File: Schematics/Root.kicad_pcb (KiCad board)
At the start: 2 copper layers, 100 x 100 mm, 132 parts, among them CON1 USB-MICRO-B, IC1 ATXMEGA256A3BU-A, J1 AVR_JTAG_Header, P1 CONN_02X08, U1 PCA9685, U10 PCA9685, U11 PCA9685, U12 PCA9685, U13 LT8612, U2 PCA9685, U3 PCA9685, U4 PCA9685, U5 PCA9685, U6 PCA9685, U7 PCA9685, U8 PCA9685, U9 PCA9685, X1 12MHz, X2 32.768KhZ

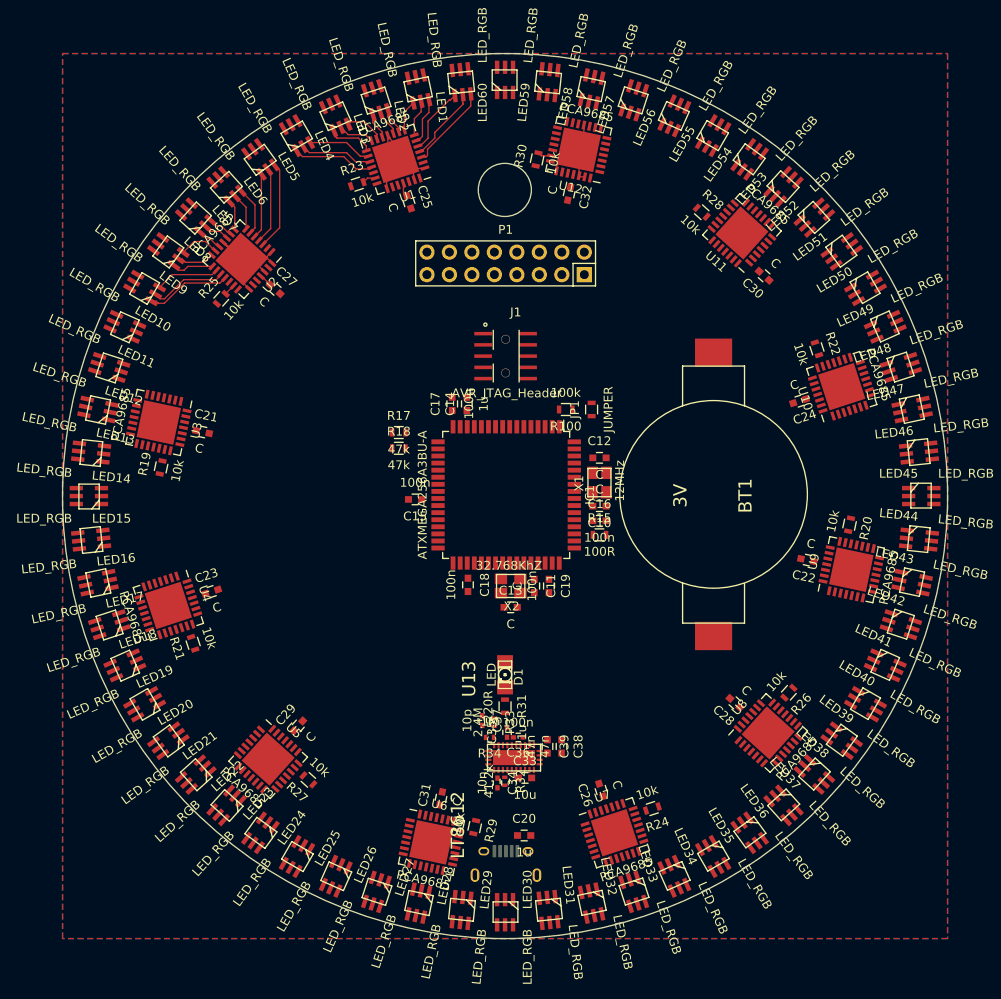
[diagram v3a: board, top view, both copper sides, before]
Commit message: Changed lots
Finalised the Inductor. Closes #5
Changed USB Connector. Closes #4
Added four switches for a simple interface. Closes #7
Added a power jack. Closes #3
Found RTC Oscillator. Closes #1.
Added part numbers to all major components. Closes #2
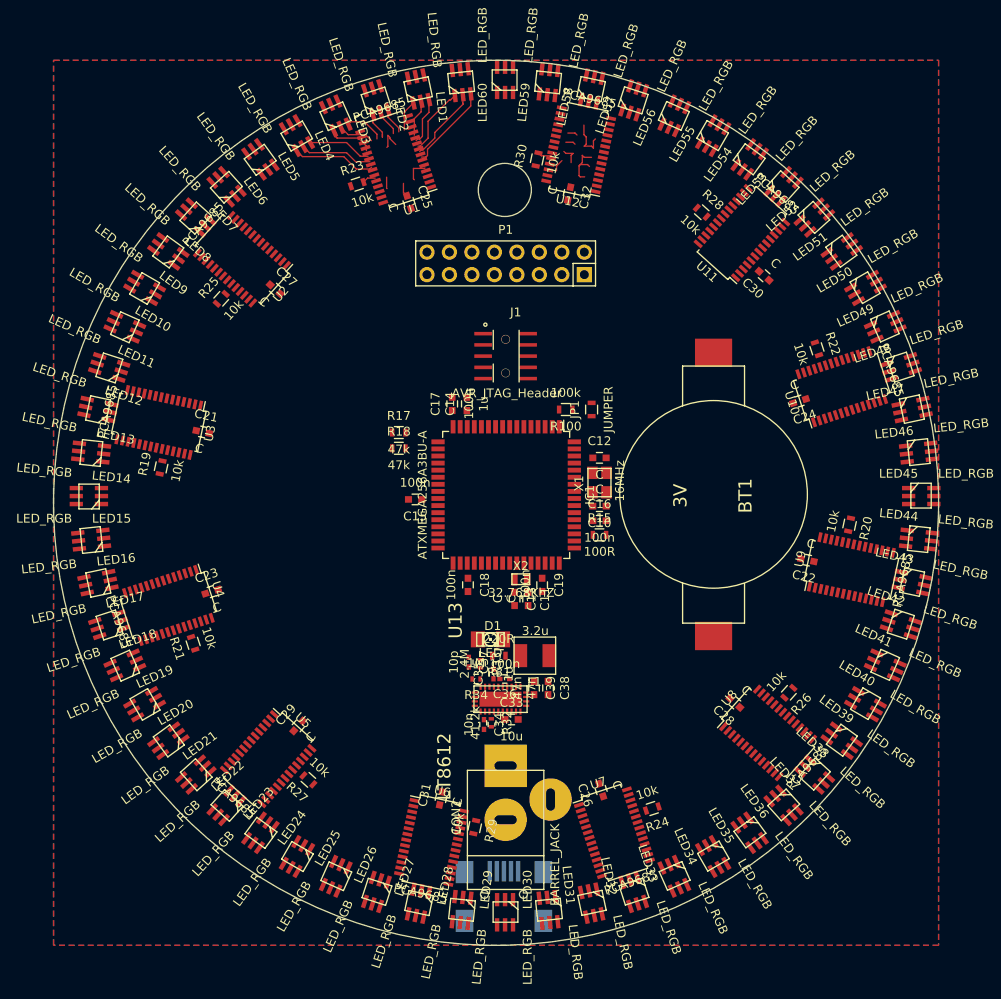
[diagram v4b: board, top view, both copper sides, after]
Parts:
- removed C20: 1u, Capacitors_SMD:C_0603
- added CON2: BARREL_JACK, Connect:JACK_ALIM, F.Cu at (105.6, 121.8)
- added L1: 3.2u, rgb:SD43, F.Cu at (108.9, 103.2)
- CON1: footprint usb:USB_Micro-B -> Connect:USB_Mini-B
- U1, U10, U11, U12, U2, U3, U4, U5, U6, U7, U8, U9: footprint Housings_DFN_QFN:QFN-28-1EP_6x6mm_Pitch0.65mm -> Housings_SSOP:TSSOP-28_4.4x9.7mm_Pitch0.65mm
- X1: value 12MHz -> 16MHz
- X2: footprint Crystals_Oscillators_SMD:crystal_FA238-TSX3225 -> rgb:SMD_Osc
- moved C35 6.78 mm to (104.2, 105.3)
- moved C33 6.78 mm to (106.2, 110.4)
- moved C34 6.78 mm to (103.1, 111.0)
- moved C36 6.78 mm to (105.5, 105.9)
- moved C37 6.78 mm to (101.4, 104.0)
- moved C38 6.78 mm to (110.4, 106.9)
- moved C39 6.78 mm to (108.8, 106.9)
- moved R32 6.78 mm to (103.9, 110.8)
- moved R33 6.78 mm to (102.7, 104.2)
- moved R34 6.78 mm to (102.2, 105.9)
- moved U13 6.78 mm to (105.0, 108.1)
- moved CON1 5.91 mm to (105.4, 131.0)
- moved R31 5.76 mm to (104.8, 103.2), turned to 180 degrees
- moved D1 4.33 mm to (103.8, 101.4), turned to 0 degrees
- moved C11 1.62 mm to (108.1, 96.8)
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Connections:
- CON1 pad 1: /Power Supply/Vin -> Net-(CON1-Pad1)
- U1 pad 1: GND -> VPP
- U1 pad 10: Net-(LED3-PadGC) -> Net-(LED2-PadGC)
- U1 pad 11: GND -> Net-(LED2-PadBC)
- U1 pad 12: Net-(LED3-PadBC) -> Net-(LED3-PadRC)
- U1 pad 13: Net-(LED4-PadRC) -> Net-(LED3-PadGC)
- U1 pad 14: Net-(LED4-PadGC) -> GND
- U1 pad 15: Net-(LED4-PadBC) -> Net-(LED3-PadBC)
- U1 pad 16: Net-(LED5-PadRC) -> Net-(LED4-PadRC)
- U1 pad 17: Net-(LED5-PadGC) -> Net-(LED4-PadGC)
- U1 pad 18: Net-(LED5-PadBC) -> Net-(LED4-PadBC)
- U1 pad 19: Net-(U1-Pad19) -> Net-(LED5-PadRC)
- U1 pad 2: VPP -> GND
- U1 pad 20: /Display/Display Sub block 1/~OE -> Net-(LED5-PadGC)
- U1 pad 21: VPP -> Net-(LED5-PadBC)
- U1 pad 22: GND -> Net-(U1-Pad22)
- U1 pad 23: /Display/SCL -> /Display/Display Sub block 1/~OE
- U1 pad 24: /Display/SDA -> VPP
- U1 pad 25: VPP -> GND
- U1 pad 26: VPP -> /Display/SCL
- U1 pad 27: GND -> /Display/SDA
- U1 pad 28: GND -> VPP
- U1 pad 3: Net-(LED1-PadRC) -> GND
- U1 pad 4: Net-(LED1-PadGC) -> GND
- U1 pad 5: Net-(LED1-PadBC) -> VPP
- U1 pad 6: Net-(LED2-PadRC) -> Net-(LED1-PadRC)
- U1 pad 7: Net-(LED2-PadGC) -> Net-(LED1-PadGC)
- U1 pad 8: Net-(LED2-PadBC) -> Net-(LED1-PadBC)
- U1 pad 9: Net-(LED3-PadRC) -> Net-(LED2-PadRC)
- U10 pad 1: VPP -> GND
- U10 pad 10: Net-(LED48-PadGC) -> Net-(LED47-PadGC)
- U10 pad 11: GND -> Net-(LED47-PadBC)
- U10 pad 12: Net-(LED48-PadBC) -> Net-(LED48-PadRC)
- U10 pad 13: Net-(LED49-PadRC) -> Net-(LED48-PadGC)
- U10 pad 14: Net-(LED49-PadGC) -> GND
- U10 pad 15: Net-(LED49-PadBC) -> Net-(LED48-PadBC)
- U10 pad 16: Net-(LED50-PadRC) -> Net-(LED49-PadRC)
- U10 pad 17: Net-(LED50-PadGC) -> Net-(LED49-PadGC)
- U10 pad 18: Net-(LED50-PadBC) -> Net-(LED49-PadBC)
- U10 pad 19: Net-(U10-Pad19) -> Net-(LED50-PadRC)
- U10 pad 20: /Display/Display Sub block 10/~OE -> Net-(LED50-PadGC)
- U10 pad 21: VPP -> Net-(LED50-PadBC)
- U10 pad 22: GND -> Net-(U10-Pad22)
- U10 pad 23: /Display/SCL -> /Display/Display Sub block 10/~OE
- U10 pad 24: /Display/SDA -> VPP
- U10 pad 25: VPP -> GND
- U10 pad 26: GND -> /Display/SCL
- U10 pad 27: VPP -> /Display/SDA
- U10 pad 28: GND -> VPP
- U10 pad 3: Net-(LED46-PadRC) -> GND
- U10 pad 4: Net-(LED46-PadGC) -> VPP
- U10 pad 5: Net-(LED46-PadBC) -> VPP
- U10 pad 6: Net-(LED47-PadRC) -> Net-(LED46-PadRC)
- U10 pad 7: Net-(LED47-PadGC) -> Net-(LED46-PadGC)
- U10 pad 8: Net-(LED47-PadBC) -> Net-(LED46-PadBC)
- U10 pad 9: Net-(LED48-PadRC) -> Net-(LED47-PadRC)
- U11 pad 10: Net-(LED53-PadGC) -> Net-(LED52-PadGC)
- U11 pad 11: GND -> Net-(LED52-PadBC)
- U11 pad 12: Net-(LED53-PadBC) -> Net-(LED53-PadRC)
- U11 pad 13: Net-(LED54-PadRC) -> Net-(LED53-PadGC)
- U11 pad 14: Net-(LED54-PadGC) -> GND
- U11 pad 15: Net-(LED54-PadBC) -> Net-(LED53-PadBC)
- U11 pad 16: Net-(LED55-PadRC) -> Net-(LED54-PadRC)
- U11 pad 17: Net-(LED55-PadGC) -> Net-(LED54-PadGC)
- U11 pad 18: Net-(LED55-PadBC) -> Net-(LED54-PadBC)
- U11 pad 19: Net-(U11-Pad19) -> Net-(LED55-PadRC)
- U11 pad 20: /Display/Display Sub block 11/~OE -> Net-(LED55-PadGC)
- U11 pad 21: VPP -> Net-(LED55-PadBC)
- U11 pad 22: GND -> Net-(U11-Pad22)
- U11 pad 23: /Display/SCL -> /Display/Display Sub block 11/~OE
- U11 pad 24: /Display/SDA -> VPP
- U11 pad 25: VPP -> GND
- U11 pad 26: VPP -> /Display/SCL
- U11 pad 27: VPP -> /Display/SDA
- U11 pad 28: GND -> VPP
- U11 pad 3: Net-(LED51-PadRC) -> GND
- U11 pad 4: Net-(LED51-PadGC) -> VPP
- U11 pad 5: Net-(LED51-PadBC) -> VPP
- U11 pad 6: Net-(LED52-PadRC) -> Net-(LED51-PadRC)
- U11 pad 7: Net-(LED52-PadGC) -> Net-(LED51-PadGC)
- U11 pad 8: Net-(LED52-PadBC) -> Net-(LED51-PadBC)
- U11 pad 9: Net-(LED53-PadRC) -> Net-(LED52-PadRC)
- U12 pad 1: VPP -> GND
- U12 pad 10: Net-(LED58-PadGC) -> Net-(LED57-PadGC)
- U12 pad 11: GND -> Net-(LED57-PadBC)
- U12 pad 12: Net-(LED58-PadBC) -> Net-(LED58-PadRC)
- U12 pad 13: Net-(LED59-PadRC) -> Net-(LED58-PadGC)
- U12 pad 14: Net-(LED59-PadGC) -> GND
- U12 pad 15: Net-(LED59-PadBC) -> Net-(LED58-PadBC)
- U12 pad 16: Net-(LED60-PadRC) -> Net-(LED59-PadRC)
- U12 pad 17: Net-(LED60-PadGC) -> Net-(LED59-PadGC)
- U12 pad 18: Net-(LED60-PadBC) -> Net-(LED59-PadBC)
- U12 pad 19: Net-(U12-Pad19) -> Net-(LED60-PadRC)
- U12 pad 2: VPP -> GND
- U12 pad 20: /Display/Display Sub block 12/~OE -> Net-(LED60-PadGC)
- U12 pad 21: VPP -> Net-(LED60-PadBC)
- U12 pad 22: GND -> Net-(U12-Pad22)
- U12 pad 23: /Display/SCL -> /Display/Display Sub block 12/~OE
- U12 pad 24: /Display/SDA -> VPP
- U12 pad 25: VPP -> GND
- U12 pad 26: GND -> /Display/SCL
- U12 pad 27: GND -> /Display/SDA
- U12 pad 3: Net-(LED56-PadRC) -> VPP
- U12 pad 4: Net-(LED56-PadGC) -> VPP
- U12 pad 5: Net-(LED56-PadBC) -> VPP
- U12 pad 6: Net-(LED57-PadRC) -> Net-(LED56-PadRC)
- U12 pad 7: Net-(LED57-PadGC) -> Net-(LED56-PadGC)
- U12 pad 8: Net-(LED57-PadBC) -> Net-(LED56-PadBC)
- U12 pad 9: Net-(LED58-PadRC) -> Net-(LED57-PadRC)
- U2 pad 10: Net-(LED8-PadGC) -> Net-(LED7-PadGC)
- U2 pad 11: GND -> Net-(LED7-PadBC)
- U2 pad 12: Net-(LED8-PadBC) -> Net-(LED8-PadRC)
- U2 pad 13: Net-(LED9-PadRC) -> Net-(LED8-PadGC)
- U2 pad 14: Net-(LED9-PadGC) -> GND
- U2 pad 15: Net-(LED9-PadBC) -> Net-(LED8-PadBC)
- U2 pad 16: Net-(LED10-PadRC) -> Net-(LED9-PadRC)
- U2 pad 17: Net-(LED10-PadGC) -> Net-(LED9-PadGC)
- U2 pad 18: Net-(LED10-PadBC) -> Net-(LED9-PadBC)
- U2 pad 19: Net-(U2-Pad19) -> Net-(LED10-PadRC)
- U2 pad 20: /Display/Display Sub block 2/~OE -> Net-(LED10-PadGC)
- U2 pad 21: VPP -> Net-(LED10-PadBC)
- U2 pad 22: GND -> Net-(U2-Pad22)
- U2 pad 23: /Display/SCL -> /Display/Display Sub block 2/~OE
- U2 pad 24: /Display/SDA -> VPP
- U2 pad 25: VPP -> GND
- U2 pad 26: GND -> /Display/SCL
- U2 pad 27: VPP -> /Display/SDA
- U2 pad 28: GND -> VPP
- U2 pad 3: Net-(LED6-PadRC) -> GND
- U2 pad 4: Net-(LED6-PadGC) -> GND
- U2 pad 5: Net-(LED6-PadBC) -> VPP
- U2 pad 6: Net-(LED7-PadRC) -> Net-(LED6-PadRC)
- U2 pad 7: Net-(LED7-PadGC) -> Net-(LED6-PadGC)
- U2 pad 8: Net-(LED7-PadBC) -> Net-(LED6-PadBC)
- U2 pad 9: Net-(LED8-PadRC) -> Net-(LED7-PadRC)
- U3 pad 1: GND -> VPP
- U3 pad 10: Net-(LED13-PadGC) -> Net-(LED12-PadGC)
- U3 pad 11: GND -> Net-(LED12-PadBC)
- U3 pad 12: Net-(LED13-PadBC) -> Net-(LED13-PadRC)
- U3 pad 13: Net-(LED14-PadRC) -> Net-(LED13-PadGC)
- U3 pad 14: Net-(LED14-PadGC) -> GND
- U3 pad 15: Net-(LED14-PadBC) -> Net-(LED13-PadBC)
- U3 pad 16: Net-(LED15-PadRC) -> Net-(LED14-PadRC)
- U3 pad 17: Net-(LED15-PadGC) -> Net-(LED14-PadGC)
- U3 pad 18: Net-(LED15-PadBC) -> Net-(LED14-PadBC)
- U3 pad 19: Net-(U3-Pad19) -> Net-(LED15-PadRC)
- U3 pad 20: /Display/Display Sub block 3/~OE -> Net-(LED15-PadGC)
- U3 pad 21: VPP -> Net-(LED15-PadBC)
- U3 pad 22: GND -> Net-(U3-Pad22)
- U3 pad 23: /Display/SCL -> /Display/Display Sub block 3/~OE
- U3 pad 24: /Display/SDA -> VPP
- U3 pad 25: VPP -> GND
- U3 pad 26: VPP -> /Display/SCL
- U3 pad 27: VPP -> /Display/SDA
- U3 pad 28: GND -> VPP
- U3 pad 3: Net-(LED11-PadRC) -> GND
- U3 pad 4: Net-(LED11-PadGC) -> GND
- U3 pad 5: Net-(LED11-PadBC) -> VPP
- U3 pad 6: Net-(LED12-PadRC) -> Net-(LED11-PadRC)
- U3 pad 7: Net-(LED12-PadGC) -> Net-(LED11-PadGC)
- U3 pad 8: Net-(LED12-PadBC) -> Net-(LED11-PadBC)
- U3 pad 9: Net-(LED13-PadRC) -> Net-(LED12-PadRC)
- U4 pad 10: Net-(LED18-PadGC) -> Net-(LED17-PadGC)
- U4 pad 11: GND -> Net-(LED17-PadBC)
- U4 pad 12: Net-(LED18-PadBC) -> Net-(LED18-PadRC)
- U4 pad 13: Net-(LED19-PadRC) -> Net-(LED18-PadGC)
- U4 pad 14: Net-(LED19-PadGC) -> GND
- U4 pad 15: Net-(LED19-PadBC) -> Net-(LED18-PadBC)
- U4 pad 16: Net-(LED20-PadRC) -> Net-(LED19-PadRC)
- U4 pad 17: Net-(LED20-PadGC) -> Net-(LED19-PadGC)
- U4 pad 18: Net-(LED20-PadBC) -> Net-(LED19-PadBC)
- U4 pad 19: Net-(U4-Pad19) -> Net-(LED20-PadRC)
- U4 pad 2: VPP -> GND
- U4 pad 20: /Display/Display Sub block 4/~OE -> Net-(LED20-PadGC)
- U4 pad 21: VPP -> Net-(LED20-PadBC)
- U4 pad 22: GND -> Net-(U4-Pad22)
- U4 pad 23: /Display/SCL -> /Display/Display Sub block 4/~OE
- U4 pad 24: /Display/SDA -> VPP
- U4 pad 25: VPP -> GND
- U4 pad 26: GND -> /Display/SCL
- U4 pad 27: GND -> /Display/SDA
- U4 pad 3: Net-(LED16-PadRC) -> VPP
- U4 pad 4: Net-(LED16-PadGC) -> GND
- U4 pad 5: Net-(LED16-PadBC) -> VPP
- U4 pad 6: Net-(LED17-PadRC) -> Net-(LED16-PadRC)
- U4 pad 7: Net-(LED17-PadGC) -> Net-(LED16-PadGC)
- U4 pad 8: Net-(LED17-PadBC) -> Net-(LED16-PadBC)
- U4 pad 9: Net-(LED18-PadRC) -> Net-(LED17-PadRC)
- U5 pad 1: GND -> VPP
- U5 pad 10: Net-(LED23-PadGC) -> Net-(LED22-PadGC)
- U5 pad 11: GND -> Net-(LED22-PadBC)
- U5 pad 12: Net-(LED23-PadBC) -> Net-(LED23-PadRC)
- U5 pad 13: Net-(LED24-PadRC) -> Net-(LED23-PadGC)
- U5 pad 14: Net-(LED24-PadGC) -> GND
- U5 pad 15: Net-(LED24-PadBC) -> Net-(LED23-PadBC)
- U5 pad 16: Net-(LED25-PadRC) -> Net-(LED24-PadRC)
- U5 pad 17: Net-(LED25-PadGC) -> Net-(LED24-PadGC)
- U5 pad 18: Net-(LED25-PadBC) -> Net-(LED24-PadBC)
- U5 pad 19: Net-(U5-Pad19) -> Net-(LED25-PadRC)
- U5 pad 2: VPP -> GND
- U5 pad 20: /Display/Display Sub block 5/~OE -> Net-(LED25-PadGC)
- U5 pad 21: VPP -> Net-(LED25-PadBC)
- U5 pad 22: GND -> Net-(U5-Pad22)
- U5 pad 23: /Display/SCL -> /Display/Display Sub block 5/~OE
- U5 pad 24: /Display/SDA -> VPP
- U5 pad 25: VPP -> GND
- U5 pad 26: VPP -> /Display/SCL
- U5 pad 27: GND -> /Display/SDA
- U5 pad 3: Net-(LED21-PadRC) -> VPP
- U5 pad 4: Net-(LED21-PadGC) -> GND
- U5 pad 5: Net-(LED21-PadBC) -> VPP
- U5 pad 6: Net-(LED22-PadRC) -> Net-(LED21-PadRC)
- U5 pad 7: Net-(LED22-PadGC) -> Net-(LED21-PadGC)
- U5 pad 8: Net-(LED22-PadBC) -> Net-(LED21-PadBC)
- U5 pad 9: Net-(LED23-PadRC) -> Net-(LED22-PadRC)
- U6 pad 10: Net-(LED28-PadGC) -> Net-(LED27-PadGC)
- U6 pad 11: GND -> Net-(LED27-PadBC)
- U6 pad 12: Net-(LED28-PadBC) -> Net-(LED28-PadRC)
- U6 pad 13: Net-(LED29-PadRC) -> Net-(LED28-PadGC)
- U6 pad 14: Net-(LED29-PadGC) -> GND
- U6 pad 15: Net-(LED29-PadBC) -> Net-(LED28-PadBC)
- U6 pad 16: Net-(LED30-PadRC) -> Net-(LED29-PadRC)
- U6 pad 17: Net-(LED30-PadGC) -> Net-(LED29-PadGC)
- U6 pad 18: Net-(LED30-PadBC) -> Net-(LED29-PadBC)
- U6 pad 19: Net-(U6-Pad19) -> Net-(LED30-PadRC)
- U6 pad 20: /Display/Display Sub block 6/~OE -> Net-(LED30-PadGC)
- U6 pad 21: VPP -> Net-(LED30-PadBC)
- U6 pad 22: GND -> Net-(U6-Pad22)
- U6 pad 23: /Display/SCL -> /Display/Display Sub block 6/~OE
- U6 pad 24: /Display/SDA -> VPP
- U6 pad 25: VPP -> GND
- U6 pad 26: GND -> /Display/SCL
- U6 pad 27: VPP -> /Display/SDA
- U6 pad 3: Net-(LED26-PadRC) -> VPP
- U6 pad 4: Net-(LED26-PadGC) -> GND
- U6 pad 5: Net-(LED26-PadBC) -> VPP
- U6 pad 6: Net-(LED27-PadRC) -> Net-(LED26-PadRC)
- U6 pad 7: Net-(LED27-PadGC) -> Net-(LED26-PadGC)
- U6 pad 8: Net-(LED27-PadBC) -> Net-(LED26-PadBC)
- U6 pad 9: Net-(LED28-PadRC) -> Net-(LED27-PadRC)
- U7 pad 1: GND -> VPP
- U7 pad 10: Net-(LED33-PadGC) -> Net-(LED32-PadGC)
- U7 pad 11: GND -> Net-(LED32-PadBC)
- U7 pad 12: Net-(LED33-PadBC) -> Net-(LED33-PadRC)
- U7 pad 13: Net-(LED34-PadRC) -> Net-(LED33-PadGC)
- U7 pad 14: Net-(LED34-PadGC) -> GND
- U7 pad 15: Net-(LED34-PadBC) -> Net-(LED33-PadBC)
- U7 pad 16: Net-(LED35-PadRC) -> Net-(LED34-PadRC)
- U7 pad 17: Net-(LED35-PadGC) -> Net-(LED34-PadGC)
- U7 pad 18: Net-(LED35-PadBC) -> Net-(LED34-PadBC)
- U7 pad 19: Net-(U7-Pad19) -> Net-(LED35-PadRC)
- U7 pad 20: /Display/Display Sub block 7/~OE -> Net-(LED35-PadGC)
- U7 pad 21: VPP -> Net-(LED35-PadBC)
- U7 pad 22: GND -> Net-(U7-Pad22)
- U7 pad 23: /Display/SCL -> /Display/Display Sub block 7/~OE
- U7 pad 24: /Display/SDA -> VPP
- U7 pad 25: VPP -> GND
- U7 pad 26: VPP -> /Display/SCL
- U7 pad 27: VPP -> /Display/SDA
- U7 pad 3: Net-(LED31-PadRC) -> VPP
- U7 pad 4: Net-(LED31-PadGC) -> GND
- U7 pad 5: Net-(LED31-PadBC) -> VPP
- U7 pad 6: Net-(LED32-PadRC) -> Net-(LED31-PadRC)
- U7 pad 7: Net-(LED32-PadGC) -> Net-(LED31-PadGC)
- U7 pad 8: Net-(LED32-PadBC) -> Net-(LED31-PadBC)
- U7 pad 9: Net-(LED33-PadRC) -> Net-(LED32-PadRC)
- U8 pad 1: VPP -> GND
- U8 pad 10: Net-(LED38-PadGC) -> Net-(LED37-PadGC)
- U8 pad 11: GND -> Net-(LED37-PadBC)
- U8 pad 12: Net-(LED38-PadBC) -> Net-(LED38-PadRC)
- U8 pad 13: Net-(LED39-PadRC) -> Net-(LED38-PadGC)
- U8 pad 14: Net-(LED39-PadGC) -> GND
- U8 pad 15: Net-(LED39-PadBC) -> Net-(LED38-PadBC)
- U8 pad 16: Net-(LED40-PadRC) -> Net-(LED39-PadRC)
- U8 pad 17: Net-(LED40-PadGC) -> Net-(LED39-PadGC)
- U8 pad 18: Net-(LED40-PadBC) -> Net-(LED39-PadBC)
- U8 pad 19: Net-(U8-Pad19) -> Net-(LED40-PadRC)
- U8 pad 2: VPP -> GND
- U8 pad 20: /Display/Display Sub block 8/~OE -> Net-(LED40-PadGC)
- U8 pad 21: VPP -> Net-(LED40-PadBC)
- U8 pad 22: GND -> Net-(U8-Pad22)
- U8 pad 23: /Display/SCL -> /Display/Display Sub block 8/~OE
- U8 pad 24: /Display/SDA -> VPP
- U8 pad 25: VPP -> GND
- U8 pad 26: GND -> /Display/SCL
- U8 pad 27: GND -> /Display/SDA
- U8 pad 28: GND -> VPP
- U8 pad 3: Net-(LED36-PadRC) -> GND
- U8 pad 4: Net-(LED36-PadGC) -> VPP
- U8 pad 5: Net-(LED36-PadBC) -> VPP
- U8 pad 6: Net-(LED37-PadRC) -> Net-(LED36-PadRC)
- U8 pad 7: Net-(LED37-PadGC) -> Net-(LED36-PadGC)
- U8 pad 8: Net-(LED37-PadBC) -> Net-(LED36-PadBC)
- U8 pad 9: Net-(LED38-PadRC) -> Net-(LED37-PadRC)
- U9 pad 10: Net-(LED43-PadGC) -> Net-(LED42-PadGC)
- U9 pad 11: GND -> Net-(LED42-PadBC)
- U9 pad 12: Net-(LED43-PadBC) -> Net-(LED43-PadRC)
- U9 pad 13: Net-(LED44-PadRC) -> Net-(LED43-PadGC)
- U9 pad 14: Net-(LED44-PadGC) -> GND
- U9 pad 15: Net-(LED44-PadBC) -> Net-(LED43-PadBC)
- U9 pad 16: Net-(LED45-PadRC) -> Net-(LED44-PadRC)
- U9 pad 17: Net-(LED45-PadGC) -> Net-(LED44-PadGC)
- U9 pad 18: Net-(LED45-PadBC) -> Net-(LED44-PadBC)
- U9 pad 19: Net-(U9-Pad19) -> Net-(LED45-PadRC)
- U9 pad 2: VPP -> GND
- U9 pad 20: /Display/Display Sub block 9/~OE -> Net-(LED45-PadGC)
- U9 pad 21: VPP -> Net-(LED45-PadBC)
- U9 pad 22: GND -> Net-(U9-Pad22)
- U9 pad 23: /Display/SCL -> /Display/Display Sub block 9/~OE
- U9 pad 24: /Display/SDA -> VPP
- U9 pad 25: VPP -> GND
- U9 pad 26: VPP -> /Display/SCL
- U9 pad 27: GND -> /Display/SDA
- U9 pad 28: GND -> VPP
- U9 pad 3: Net-(LED41-PadRC) -> GND
- U9 pad 4: Net-(LED41-PadGC) -> VPP
- U9 pad 5: Net-(LED41-PadBC) -> VPP
- U9 pad 6: Net-(LED42-PadRC) -> Net-(LED41-PadRC)
- U9 pad 7: Net-(LED42-PadGC) -> Net-(LED41-PadGC)
- U9 pad 8: Net-(LED42-PadBC) -> Net-(LED41-PadBC)
- U9 pad 9: Net-(LED43-PadRC) -> Net-(LED42-PadRC)
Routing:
- net GND: track 32.5 -> 0.00 mm
- net (no net): track 0.00 -> 23.0 mm
- net Net-(LED6-PadRC): track 10.0 -> 0.00 mm
- net Net-(LED10-PadBC): track 9.59 -> 0.00 mm
- net Net-(U1-Pad22): track 0.00 -> 8.48 mm
- net Net-(LED5-PadBC): track 9.46 -> 0.97 mm
- net Net-(LED6-PadGC): track 8.70 -> 0.46 mm
- net Net-(LED10-PadGC): track 8.81 -> 0.72 mm
- net Net-(LED6-PadBC): track 7.36 -> 0.00 mm
- net Net-(LED10-PadRC): track 7.24 -> 0.01 mm
- net Net-(LED4-PadRC): track 4.48 -> 11.1 mm
- net Net-(LED7-PadRC): track 5.61 -> 0.00 mm
- net Net-(LED9-PadBC): track 4.74 -> 0.00 mm
- net Net-(LED9-PadRC): track 4.60 -> 0.00 mm
- net Net-(LED7-PadGC): track 4.21 -> 0.00 mm
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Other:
- outline, holes or cut-outs redrawn

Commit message: Ammended a net. Done a lot of routing
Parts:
- moved D1 16.4 mm to (91.0, 111.6), turned to 90 degrees
- moved L1 16.2 mm to (92.9, 105.9), turned to 90 degrees
- moved R31 14.4 mm to (92.8, 111.1), turned to 270 degrees
- moved C38 13.4 mm to (97.2, 104.4)
- moved C30 10.9 mm to (124.7, 55.9)
- moved C39 10.8 mm to (98.3, 104.4)
- moved C36 10.6 mm to (95.3, 108.8), turned to 270 degrees
- moved C35 10.5 mm to (94.8, 110.0), turned to 180 degrees
- moved R33 10.4 mm to (95.0, 111.1), turned to 0 degrees
- moved C37 10.3 mm to (95.0, 112.0), turned to 0 degrees
- moved R34 9.89 mm to (95.5, 113.1), turned to 270 degrees
- moved U13 7.25 mm to (97.8, 109.0), turned to 180 degrees
- moved C26 7.21 mm to (123.2, 116.0), turned to 18 degrees
- moved C33 6.74 mm to (100.1, 107.7), turned to 90 degrees
- moved C29 5.37 mm to (86.3, 114.6), turned to 318 degrees
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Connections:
- IC1 pad 2: Net-(IC1-Pad2) -> /Microcontroller/JUMPER
- JP1 pad 1: Net-(JP1-Pad1) -> /Microcontroller/JUMPER
- R100 pad 2: Net-(JP1-Pad1) -> /Microcontroller/JUMPER
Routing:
- net VPP: track 1.57 -> 1092.9 mm, vias 0 -> 2
- net Net-(BT1-Pad1): track 0.00 -> 26.4 mm
- net (no net): track 23.0 -> 0.00 mm
- net /Microcontroller/~RESET: track 0.00 -> 20.0 mm, vias 0 -> 2
- net /Microcontroller/TDO: track 0.00 -> 17.6 mm
- net Net-(LED30-PadBC): track 0.00 -> 12.9 mm
- net Net-(LED31-PadRC): track 0.00 -> 12.8 mm
- net /Microcontroller/TCK: track 0.00 -> 12.3 mm
- net Net-(LED30-PadGC): track 0.00 -> 12.0 mm
- net Net-(LED31-PadGC): track 0.00 -> 11.7 mm
- net Net-(LED46-PadRC): track 0.00 -> 11.2 mm
- net Net-(LED16-PadRC): track 0.00 -> 11.0 mm
- net Net-(LED6-PadRC): track 0.00 -> 10.9 mm
- net Net-(LED56-PadRC): track 0.00 -> 10.9 mm
- net Net-(LED30-PadRC): track 0.00 -> 10.9 mm
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- added copper zone on F.Cu, net /Power Supply/SW
- added copper zone on F.Cu, net /Power Supply/Vin
- added copper zone on F.Cu, net VPP
- removed copper zone on B.Cu, net GND
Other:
- outline, holes or cut-outs redrawn
- net class Power added: clearance 0.15, trace_width 0.5, via_dia 0.3, via_drill 0.25

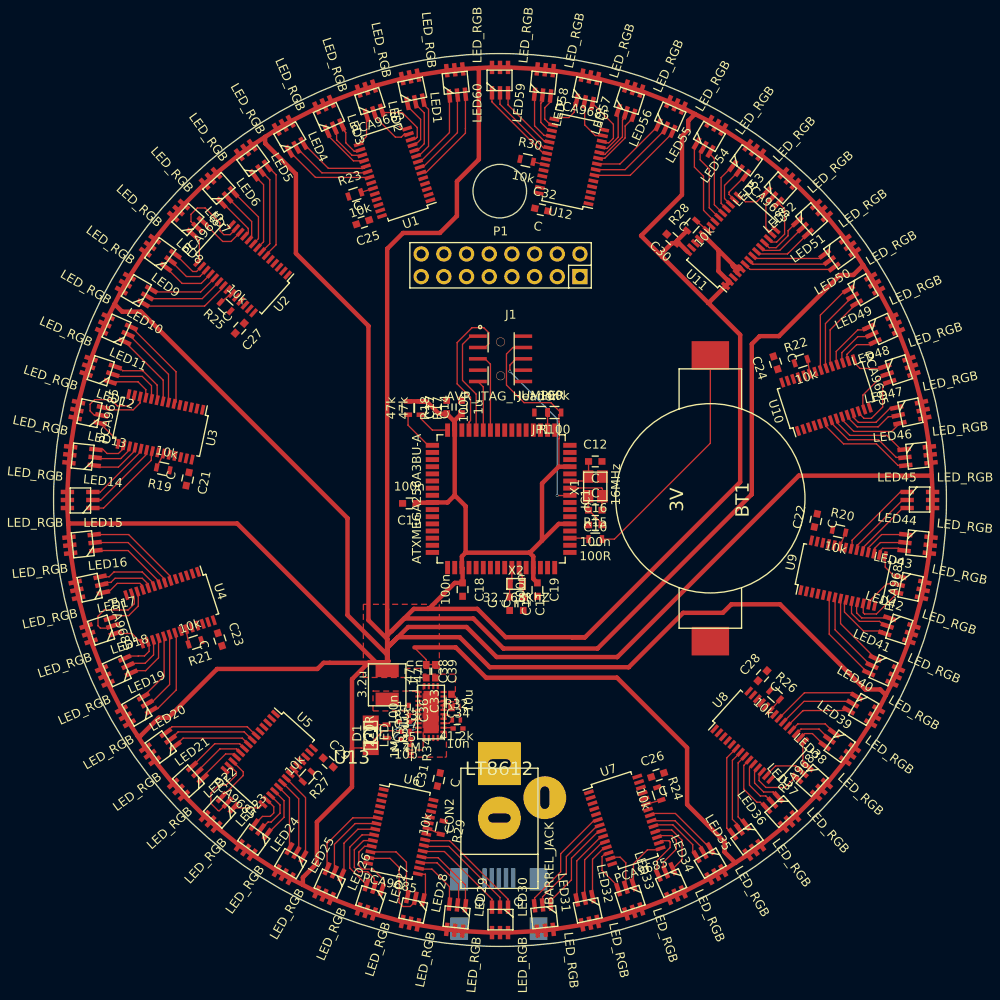
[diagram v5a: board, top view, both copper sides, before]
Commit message: Done lots of routing. Mostly done.
Rearranged some connections to make routing easier.
Need to check unconnected nets.
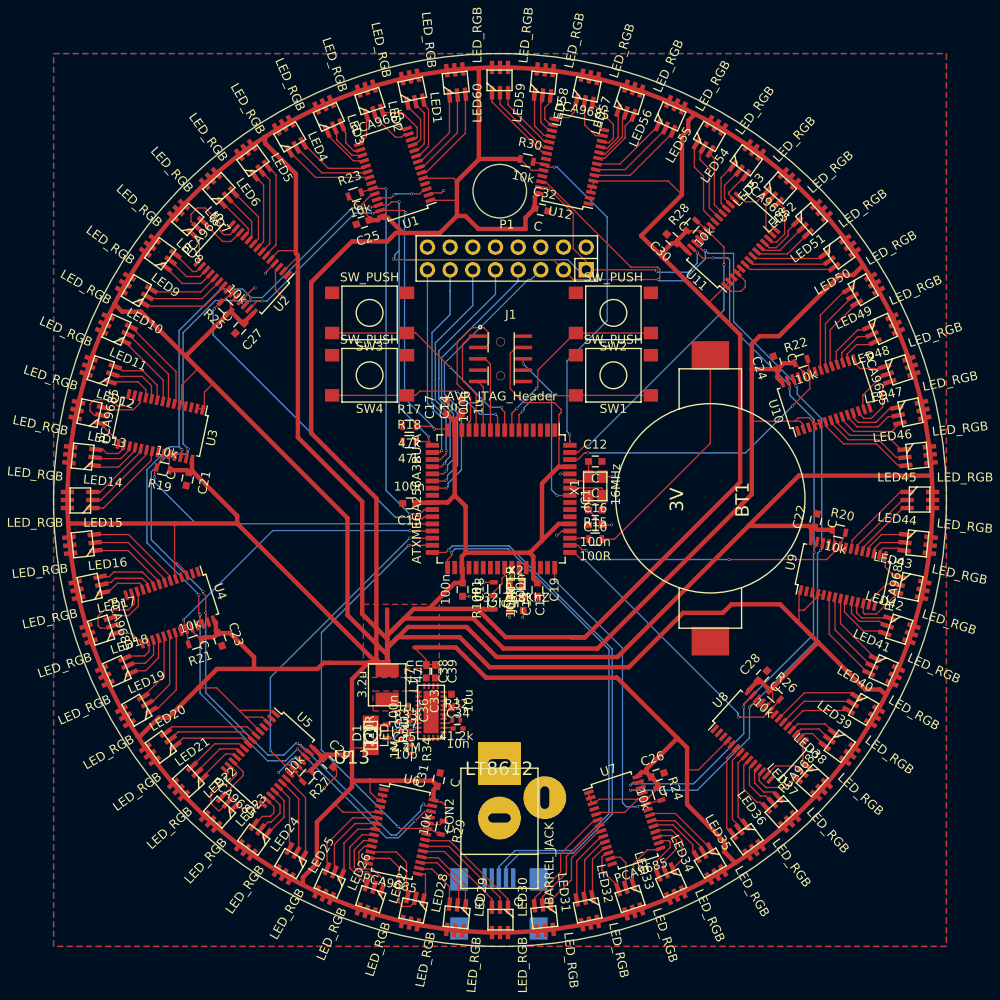
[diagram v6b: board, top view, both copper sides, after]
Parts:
- added SW1: SW_PUSH, rgb:SW, F.Cu at (118.2, 71.2)
- added SW2: SW_PUSH, rgb:SW, F.Cu at (118.2, 64.2)
- added SW3: SW_PUSH, rgb:SW, F.Cu at (90.9, 64.2)
- added SW4: SW_PUSH, rgb:SW, F.Cu at (90.9, 71.2)
- moved R100 22.4 mm to (104.8, 96.7), turned to 90 degrees
- moved JP1 20.5 mm to (104.8, 95.2), turned to 90 degrees
- moved R18 3.76 mm to (95.3, 78.7), turned to 0 degrees
- moved R17 2.40 mm to (95.3, 76.9), turned to 0 degrees
- moved P1 1.03 mm to (106.3, 58.1)
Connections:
- CON1 pad 1: Net-(CON1-Pad1) -> (no net)
- IC1 pad 1: Net-(IC1-Pad1) -> (no net)
- IC1 pad 2: /Microcontroller/JUMPER -> (no net)
- IC1 pad 26: /Display/Display Sub block 7/~OE -> /Display/Display Sub block 1/~OE
- IC1 pad 27: /Display/Display Sub block 8/~OE -> /Display/Display Sub block 2/~OE
- IC1 pad 28: /Display/Display Sub block 9/~OE -> /Display/Display Sub block 3/~OE
- IC1 pad 29: /Display/Display Sub block 10/~OE -> /Display/Display Sub block 4/~OE
- IC1 pad 3: Net-(IC1-Pad3) -> (no net)
- IC1 pad 30: /Display/Display Sub block 11/~OE -> /Display/Display Sub block 5/~OE
- IC1 pad 31: /Display/Display Sub block 12/~OE -> /Display/Display Sub block 6/~OE
- IC1 pad 36: /Display/Display Sub block 1/~OE -> (no net)
- IC1 pad 37: /Display/Display Sub block 2/~OE -> (no net)
- IC1 pad 38: /Display/Display Sub block 3/~OE -> (no net)
- IC1 pad 39: /Display/Display Sub block 4/~OE -> (no net)
- IC1 pad 4: Net-(IC1-Pad4) -> (no net)
- IC1 pad 40: /Display/Display Sub block 5/~OE -> (no net)
- IC1 pad 41: /Display/Display Sub block 6/~OE -> /Microcontroller/JUMPER
- IC1 pad 46: Net-(IC1-Pad46) -> (no net)
- IC1 pad 47: Net-(IC1-Pad47) -> (no net)
- IC1 pad 48: Net-(IC1-Pad48) -> /Display/Display Sub block 7/~OE
- IC1 pad 49: Net-(IC1-Pad49) -> /Display/Display Sub block 8/~OE
- IC1 pad 5: Net-(IC1-Pad5) -> (no net)
- IC1 pad 50: Net-(IC1-Pad50) -> /Display/Display Sub block 9/~OE
- IC1 pad 54: Net-(IC1-Pad54) -> (no net)
- IC1 pad 55: Net-(IC1-Pad55) -> (no net)
- IC1 pad 56: Net-(IC1-Pad56) -> (no net)
- IC1 pad 62: Net-(IC1-Pad62) -> /Display/Display Sub block 10/~OE
- IC1 pad 63: Net-(IC1-Pad63) -> /Display/Display Sub block 11/~OE
- IC1 pad 64: Net-(IC1-Pad64) -> /Display/Display Sub block 12/~OE
- J1 pad 7: Net-(J1-Pad7) -> (no net)
- J1 pad 8: Net-(J1-Pad8) -> (no net)
- P1 pad 11: /Microcontroller/MOSI -> /Microcontroller/~CS
- P1 pad 13: /Microcontroller/MISO -> /Microcontroller/TX
- P1 pad 15: /Microcontroller/SCK -> /Microcontroller/RX
- P1 pad 5: /Microcontroller/RX -> /Microcontroller/SCK
- P1 pad 7: /Microcontroller/TX -> /Microcontroller/MISO
- P1 pad 9: /Microcontroller/~CS -> /Microcontroller/MOSI
- U1 pad 22: Net-(U1-Pad22) -> (no net)
- U10 pad 22: Net-(U10-Pad22) -> (no net)
- U11 pad 22: Net-(U11-Pad22) -> (no net)
- U12 pad 22: Net-(U12-Pad22) -> (no net)
- U2 pad 22: Net-(U2-Pad22) -> (no net)
- U3 pad 22: Net-(U3-Pad22) -> (no net)
- U4 pad 22: Net-(U4-Pad22) -> (no net)
- U5 pad 22: Net-(U5-Pad22) -> (no net)
- U6 pad 22: Net-(U6-Pad22) -> (no net)
- U7 pad 22: Net-(U7-Pad22) -> (no net)
- U8 pad 22: Net-(U8-Pad22) -> (no net)
- U9 pad 22: Net-(U9-Pad22) -> (no net)
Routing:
- net /Display/SCL: track 4.83 -> 291.5 mm, vias 0 -> 16
- net /Display/SDA: track 3.98 -> 279.0 mm, vias 0 -> 16
- net VPP: track 1092.9 -> 1347.9 mm
- net /Microcontroller/USB_D-: track 0.00 -> 59.4 mm, vias 0 -> 1
- net /Microcontroller/USB_D+: track 0.00 -> 58.9 mm, vias 0 -> 1
- net /Display/Display Sub block 6/~OE: track 1.62 -> 46.9 mm, vias 0 -> 2
- net /Display/Display Sub block 1/~OE: track 1.74 -> 43.5 mm, vias 0 -> 2
- net /Display/Display Sub block 2/~OE: track 1.61 -> 38.8 mm, vias 0 -> 2
- net /Display/Display Sub block 12/~OE: track 1.33 -> 38.3 mm, vias 0 -> 2
- net /Display/Display Sub block 5/~OE: track 1.66 -> 38.0 mm, vias 0 -> 2
- net /Display/Display Sub block 3/~OE: track 1.74 -> 36.5 mm, vias 0 -> 2
- net /Display/Display Sub block 11/~OE: track 1.65 -> 35.2 mm, vias 0 -> 2
- net /Display/Display Sub block 4/~OE: track 1.72 -> 35.1 mm, vias 0 -> 2
- net /Display/Display Sub block 7/~OE: track 1.76 -> 34.7 mm, vias 0 -> 2
- net /Microcontroller/SCK: track 0.00 -> 32.2 mm, vias 0 -> 1
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- added copper zone on B.Cu, net GND
